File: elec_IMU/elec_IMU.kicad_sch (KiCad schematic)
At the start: 13 parts, among them J7 JST SH, U1 AS5600L

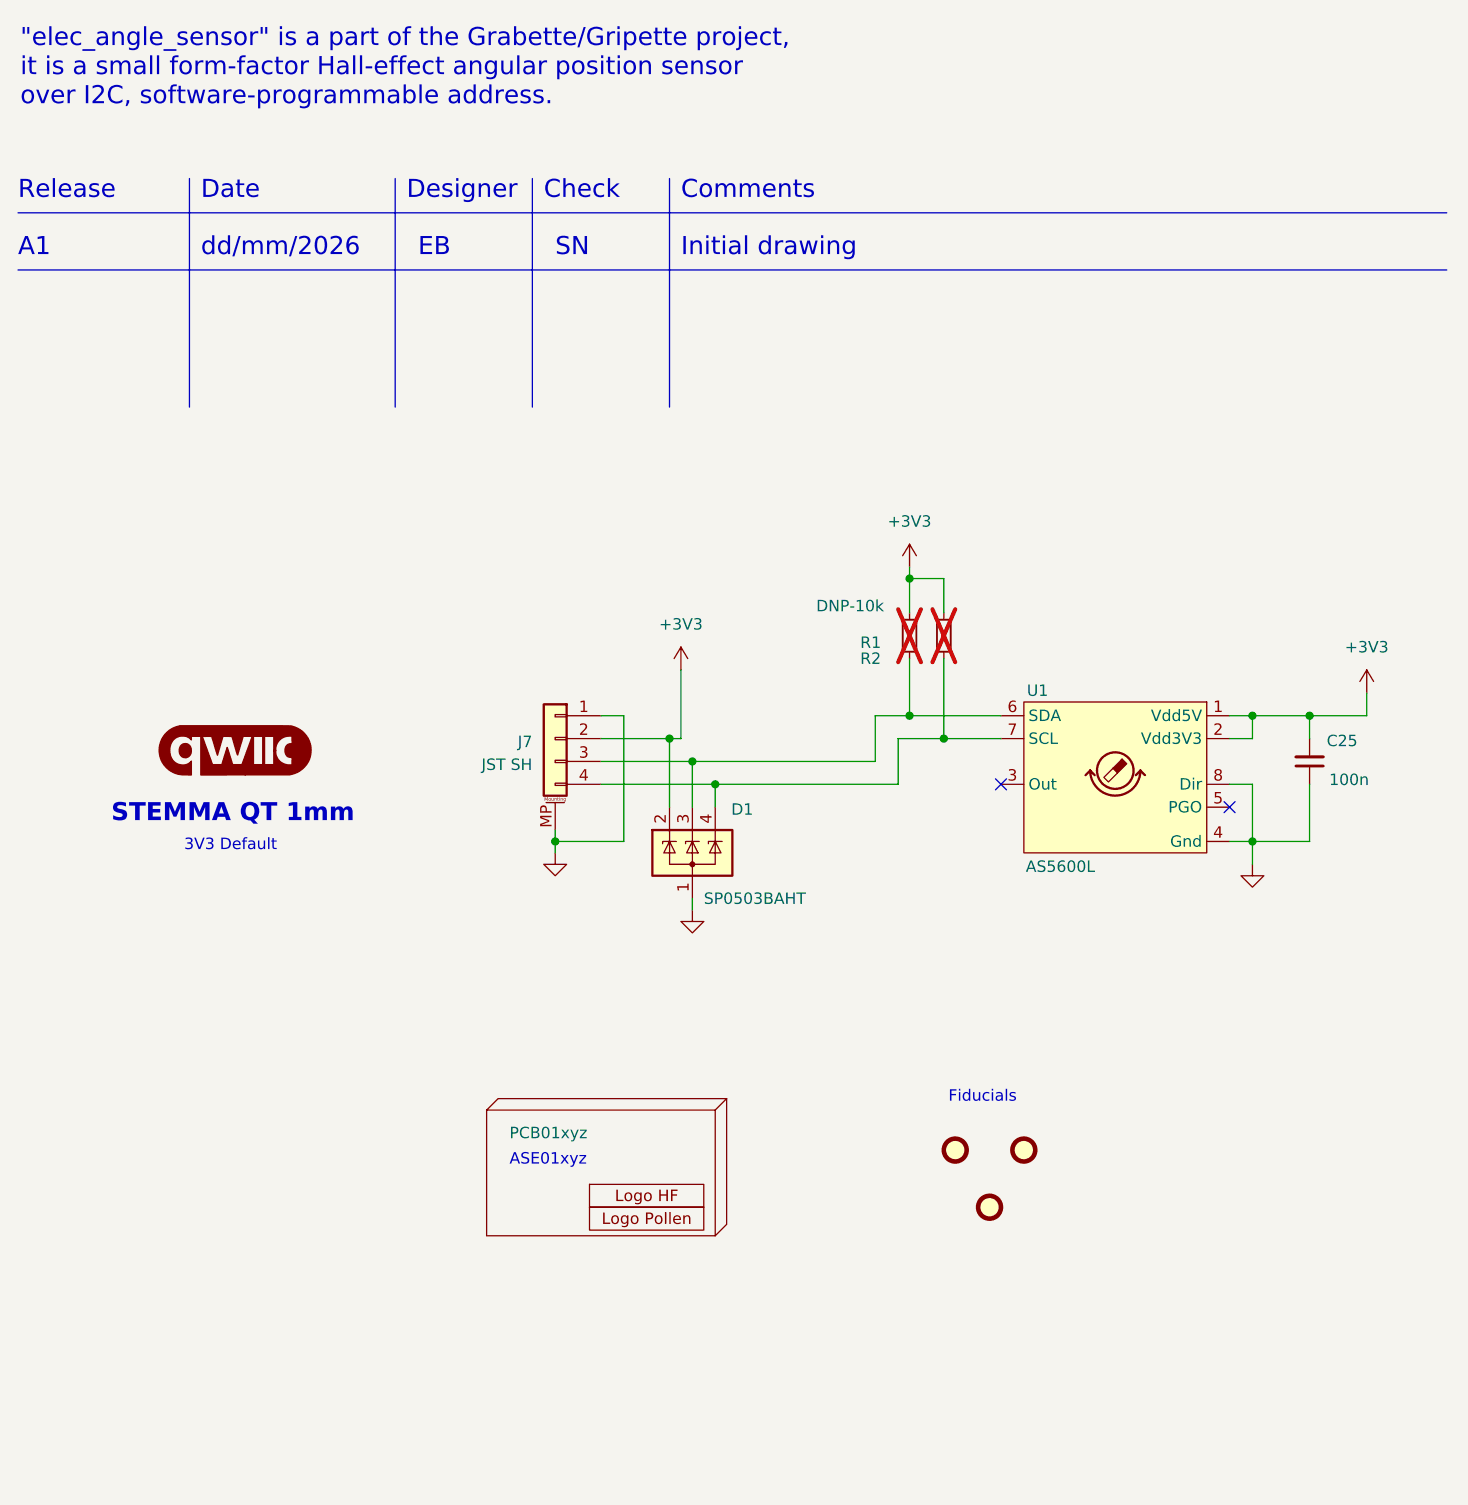
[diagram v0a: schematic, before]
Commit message: [added] elec_IMU
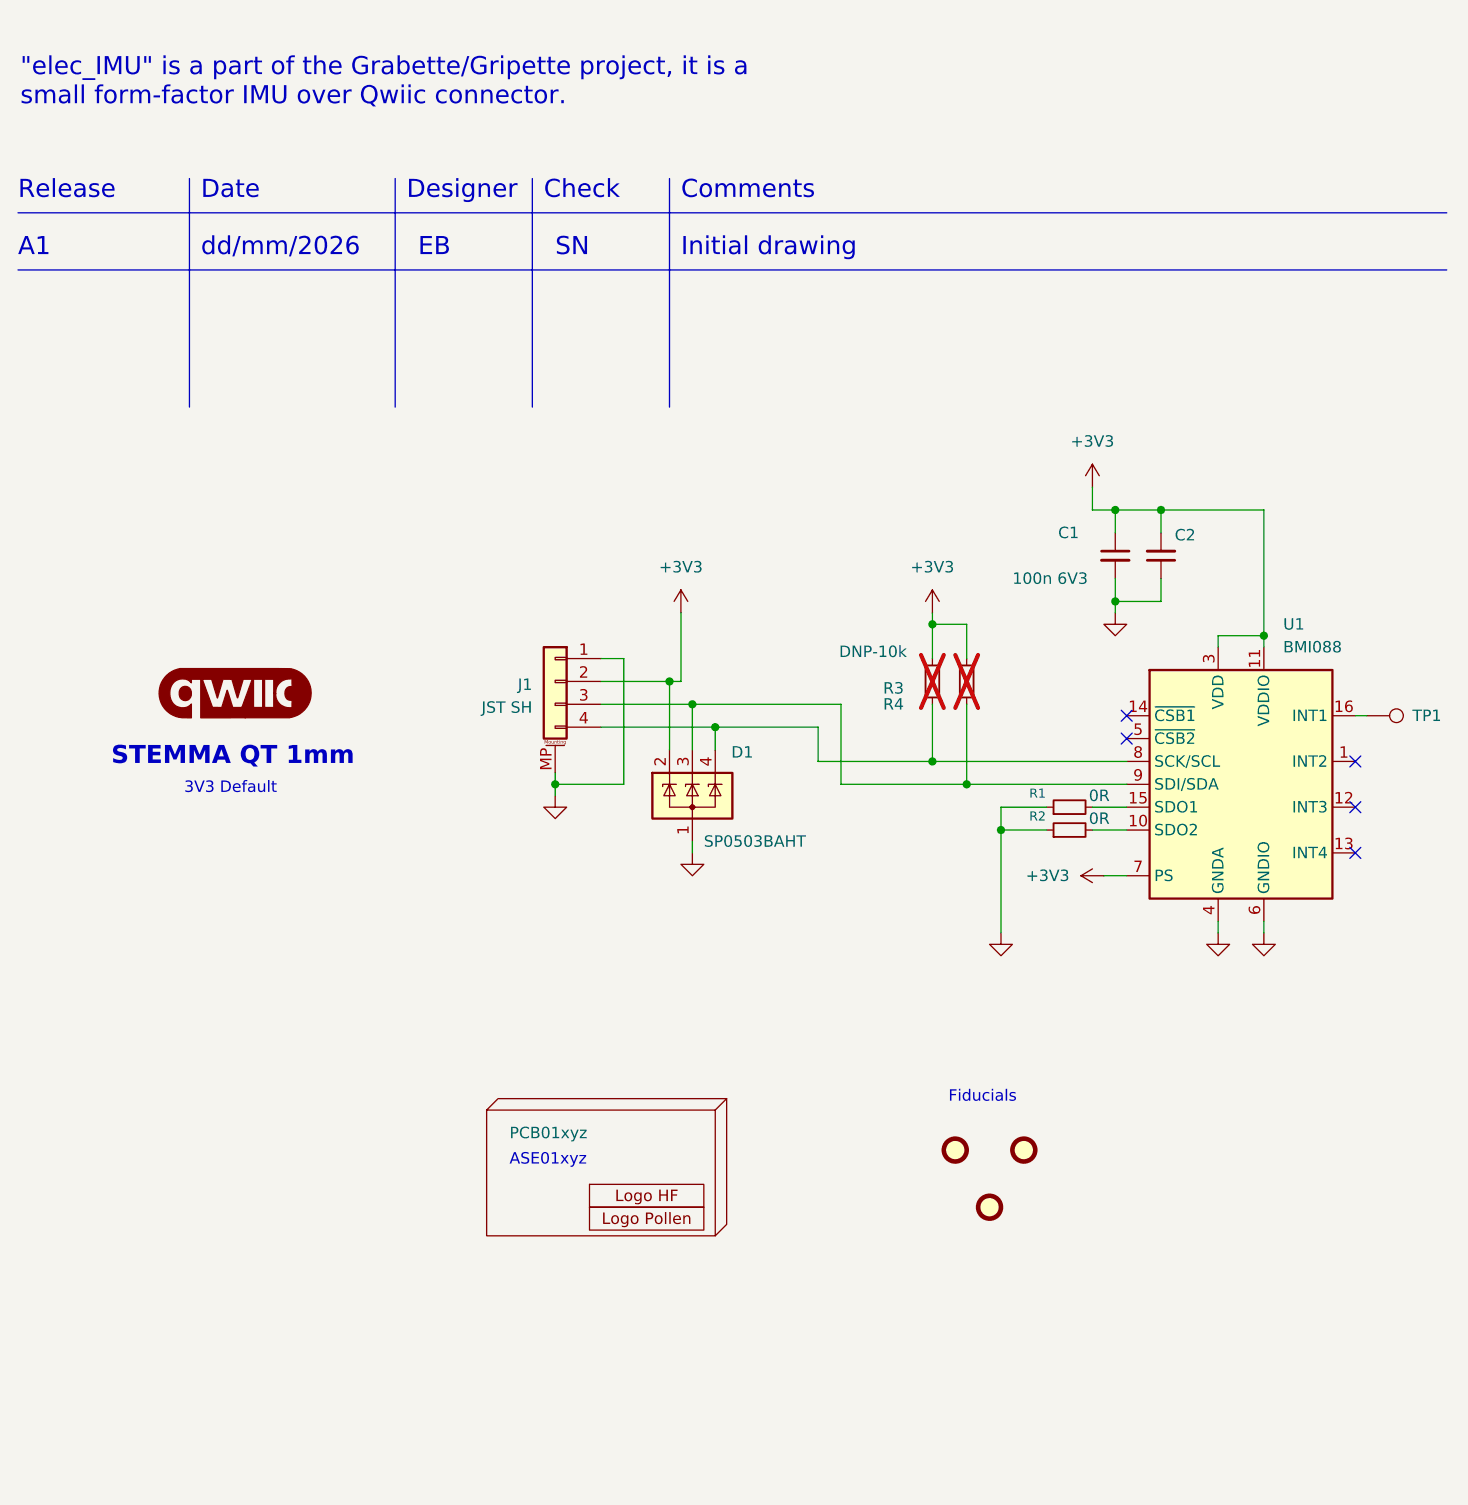
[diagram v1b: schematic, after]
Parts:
- removed C25: 100n, Capacitor_SMD:C_0402_1005Metric, symbol Device:C_Small
- removed U1: AS5600L, Package_SO:SOIC-8_3.9x4.9mm_P1.27mm, symbol Library_Pollen:AS5600L
- added C1, C2: 100n 6V3, Capacitor_SMD:C_0402_1005Metric, symbol Device:C_Small
- added R3, R4: DNP-10k, Resistor_SMD:R_0402_1005Metric, symbol Device:R_Small
- added TP1: TestPoint, TestPoint:TestPoint_Loop_D2.50mm_Drill1.0mm_LowProfile, symbol Connector:TestPoint
- added U1: BMI088, Package_LGA:Bosch_LGA-16_4.5x3mm_P0.5mm_LayoutBorder7x1y_ClockwisePinNumbering, symbol Sensor_Motion:BMI088
- R1, R2: value DNP-10k -> 0R; LCSC Part C25744 -> C17168; now fitted
- renumbered J7 to J1
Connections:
- net +3V3: now also C1.1, C2.2, R3.1, R4.1, U1.11 (VDDIO), U1.3 (VDD), U1.7 (PS); no longer R1.1, R2.1
- net GND: now also R1.1, R2.1, C1.2, C2.1, U1.2 (GNDA), U1.4 (GNDA), U1.6 (GNDIO)
- net at D1.3 (K), J1.3 (Pin_3): now also R4.2, U1.9 (SDI/SDA); no longer R1.2
- net at D1.4 (K), J1.4 (Pin_4): now also R3.2, U1.8 (SCK/SCL); no longer R2.2
- new net: R2.2, U1.10 (SDO2)
- new net: R1.2, U1.15 (SDO1)
- new net: TP1.1, U1.16 (INT1)
- no-connect marks 2 -> 5
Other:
- note added: ""elec_IMU" is a part of the Grabette/Gripette project, it is a small form-factor IMU over Qwiic connector."
- note removed: ""elec_angle_sensor" is a part of the Grabette/Gripette project, it is a small form-factor Hall-effect angular position sensor over I2C, software-programmable address."
- title: Grabette - Angle Sensor -> Grabette - IMU
- moved on the sheet: D1, J1

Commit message: [update] Full schematic + positionning
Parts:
- added H4: Mounting Holes M2,5, MountingHole:MountingHole_2.7mm_M2.5_ISO7380_Pad_TopBottom, symbol Mechanical:MountingHole_Pad
- added H5: MountingHole_Pad, MountingHole:MountingHole_2.7mm_M2.5_ISO7380_Pad_TopBottom, symbol Mechanical:MountingHole_Pad
- added H6, H7: Centering Hole 2 mm, Library_Pollen:MountingHole_2.0mm, symbol Mechanical:MountingHole
- added J2: JST SH, Connector_JST:JST_SH_SM04B-SRSS-TB_1x04-1MP_P1.00mm_Horizontal, symbol Connector_Generic_MountingPin:Conn_01x04_MountingPin
- G1: footprint Sparkfun-Qwiic:qwiic_5mm -> Library_Pollen:Logo_qwiic_5mm; symbol Sparkfun-Qwiic:qwiic_Logo -> Library_Pollen:Logo qwiic; now in the parts list
- J1: footprint Connector_JST:JST_SH_BM04B-SRSS-TB_1x04-1MP_P1.00mm_Vertical -> Connector_JST:JST_SH_SM04B-SRSS-TB_1x04-1MP_P1.00mm_Horizontal; LCSC Part C160390 -> C160404
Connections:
- net +3V3: now also J2.2 (Pin_2)
- net GND: now also H4.1, H5.1, J2.1 (Pin_1), J2.MP (MountPin)
- net at D1.4 (K), J1.4 (Pin_4), R3.2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: now also J2.4 (Pin_4)
- net at D1.3 (K), J1.3 (Pin_3), R4.2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: now also J2.3 (Pin_3)
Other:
- moved on the sheet: J1
